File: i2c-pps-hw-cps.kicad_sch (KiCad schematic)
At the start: 1 part, among them U1 BQ25758S

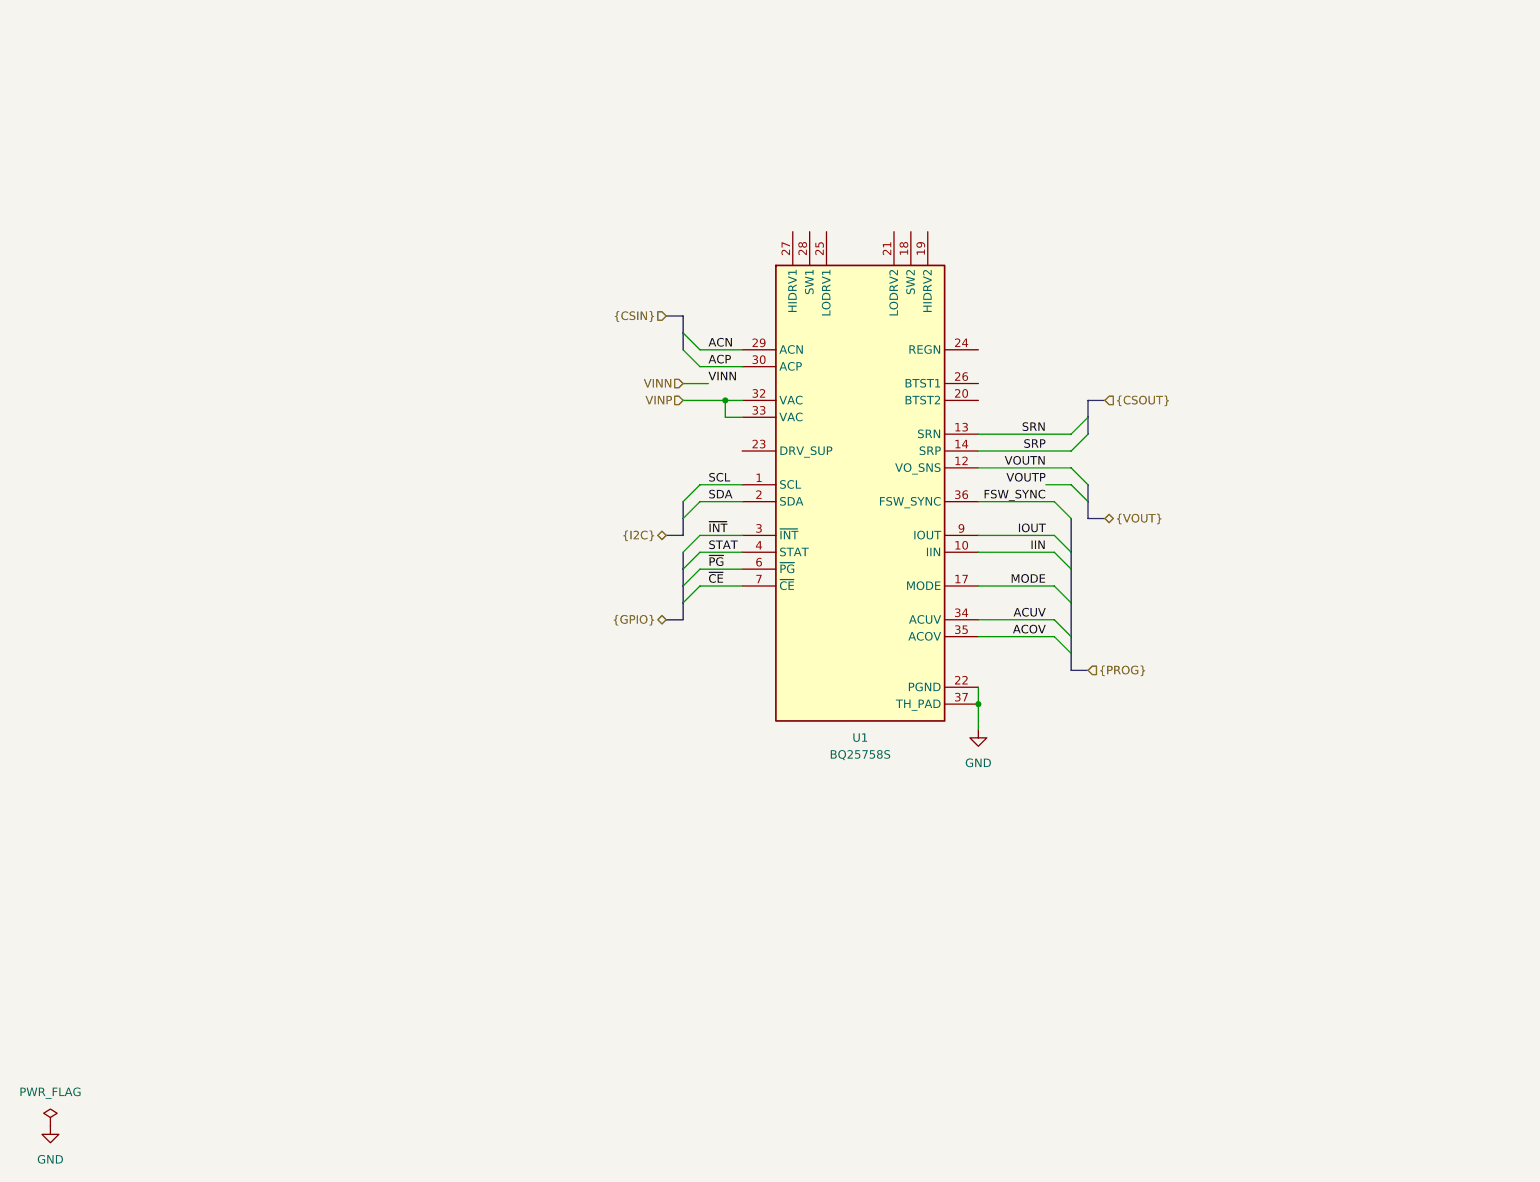
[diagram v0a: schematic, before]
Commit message: Design schematics and set per component requirements
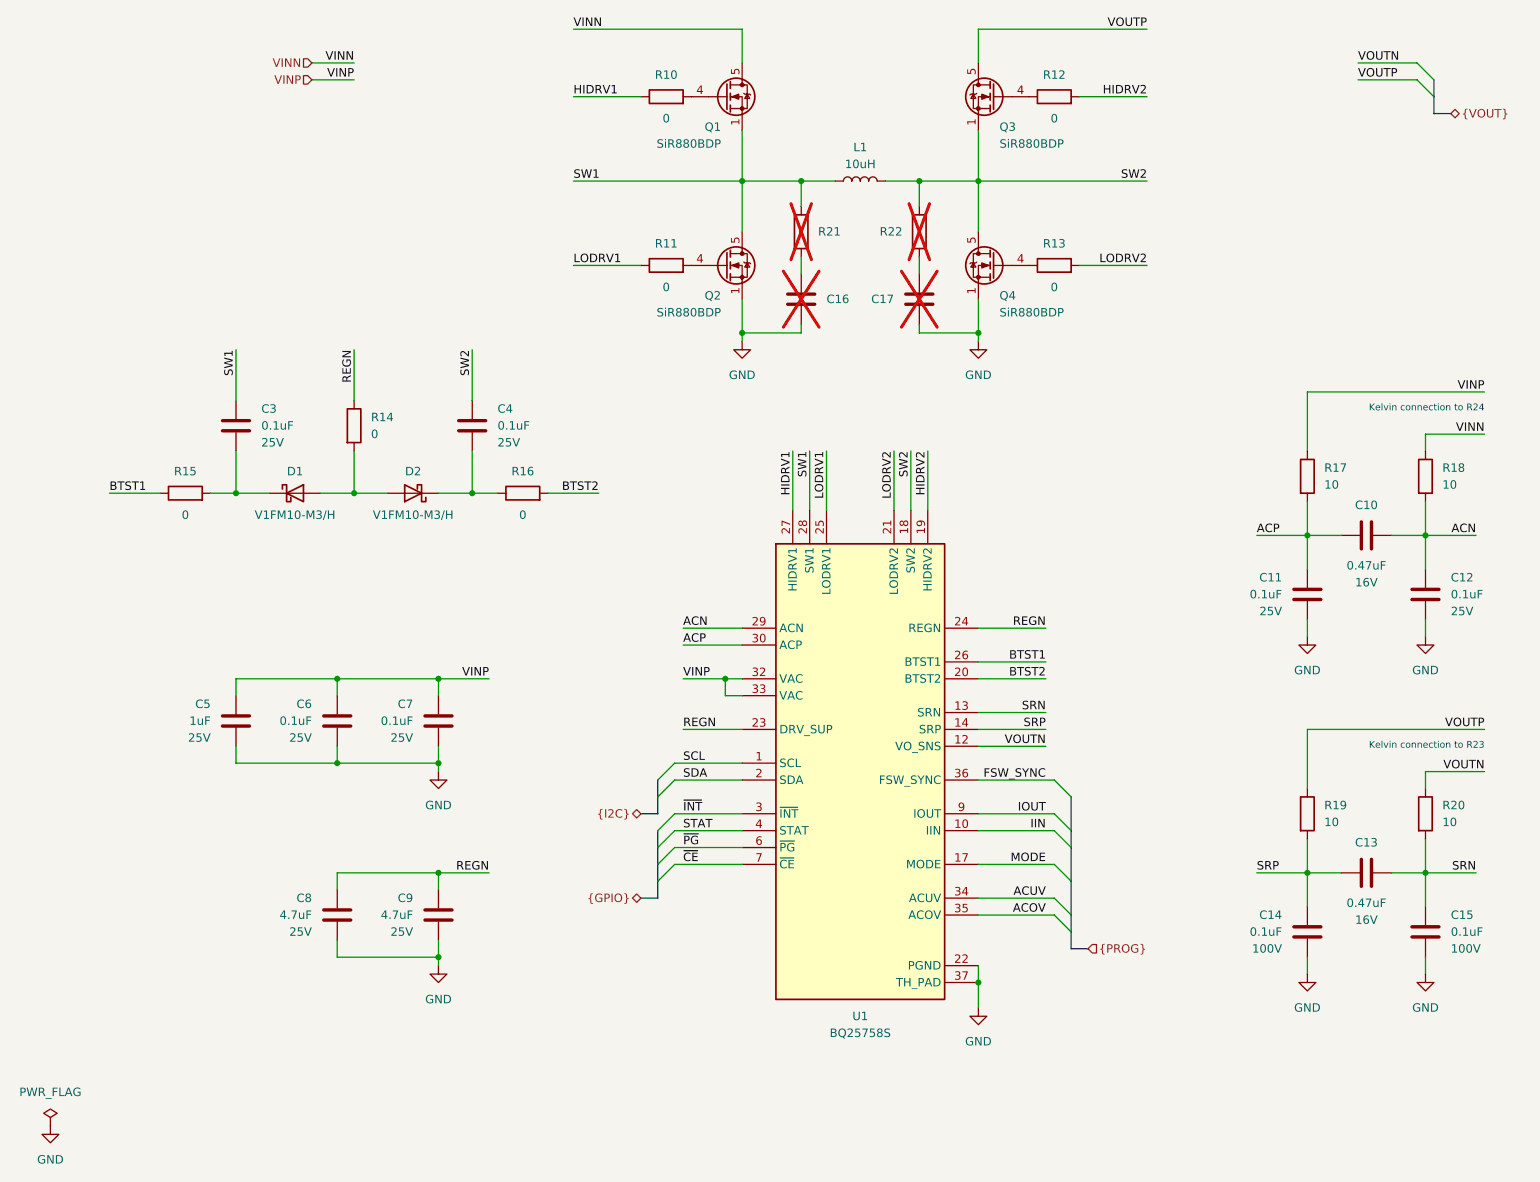
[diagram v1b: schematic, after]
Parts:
- added C10, C13: 0.47uF, Capacitor_SMD:C_0603_1608Metric_Pad1.08x0.95mm_HandSolder, symbol Device:C
- added C11, C12, C14, C15, C3, C4, C6, C7: 0.1uF, Capacitor_SMD:C_0603_1608Metric_Pad1.08x0.95mm_HandSolder, symbol Device:C
- added C16, C17: ~, Capacitor_SMD:C_0805_2012Metric, symbol Device:C
- added C5: 1uF, Capacitor_SMD:C_0805_2012Metric, symbol Device:C
- added C8, C9: 4.7uF, Capacitor_SMD:C_0805_2012Metric, symbol Device:C
- added D1, D2: V1FM10-M3/H, Diode_SMD:D_SMF, symbol Device:D_Schottky
- added L1: 10uH, symbol Device:L
- added Q1, Q2, Q3, Q4: SiR880BDP, Package_SO:PowerPAK_SO-8_Single, symbol i2c-pps-hw:SiR880BDP
- added R10, R11, R12, R13, R15, R16: 0, Resistor_SMD:R_0603_1608Metric_Pad0.98x0.95mm_HandSolder, symbol Device:R
- added R14: 0, Resistor_SMD:R_0805_2012Metric, symbol Device:R
- added R17, R18, R19, R20: 10, Resistor_SMD:R_0603_1608Metric_Pad0.98x0.95mm_HandSolder, symbol Device:R
- added R21, R22: ~, Resistor_SMD:R_1210_3225Metric, symbol Device:R
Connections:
- net ACN: now also C10.1, C12.1, R18.2
- net ACP: now also C10.2, C11.1, R17.2
- net GND: now also C11.2, C12.2, C14.2, C15.2, C16.2, C17.2, C5.2, C6.2, C7.2, C8.2, C9.2, Q2.1 (S), Q2.2 (S), Q2.3 (S), Q4.1 (S), Q4.2 (S), Q4.3 (S)
- net SRN: now also C13.1, C15.1, R20.2
- net SRP: now also C13.2, C14.1, R19.2
- net VINN: now also Q1.5 (D), R18.1
- net VINP: now also C5.1, C6.1, C7.1, R17.1
- net VOUTN: now also R20.1
- net VOUTP: now also Q3.5 (D), R19.1
- net SW2: now reaches U1.18 (SW2)
- net SW2: now also C4.1, L1.2, Q3.1 (S), Q3.2 (S), Q3.3 (S), Q4.5 (D), R22.1
- net HIDRV2: now reaches U1.19 (HIDRV2)
- net HIDRV2: now also R12.2
- net BTST2: now reaches U1.20 (BTST2)
- net BTST2: now also R16.2
- net LODRV2: now reaches U1.21 (LODRV2)
- net LODRV2: now also R13.2
- net REGN: now reaches U1.23 (DRV_SUP)
- net REGN: now also U1.24 (REGN), C8.1, C9.1, R14.1
- net LODRV1: now reaches U1.25 (LODRV1)
- net LODRV1: now also R11.1
- net BTST1: now reaches U1.26 (BTST1)
- net BTST1: now also R15.1
- net HIDRV1: now reaches U1.27 (HIDRV1)
- net HIDRV1: now also R10.1
- net SW1: now reaches U1.28 (SW1)
- net SW1: now also C3.1, L1.1, Q1.1 (S), Q1.2 (S), Q1.3 (S), Q2.5 (D), R21.1
- new net: C4.2, D2.1 (K), R16.1
- new net: D1.2 (A), D2.2 (A), R14.2
- new net: Q4.4 (G), R13.1
- new net: C3.2, D1.1 (K), R15.2
- new net: Q1.4 (G), R10.2
- new net: Q3.4 (G), R12.1
- new net: C16.1, R21.2
- new net: Q2.4 (G), R11.2
- new net: C17.1, R22.2
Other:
- note added: "Kelvin connection to R23"
- note added: "Kelvin connection to R24"
- moved on the sheet: U1

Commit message: Rename VINP to +5V_Run for clarity
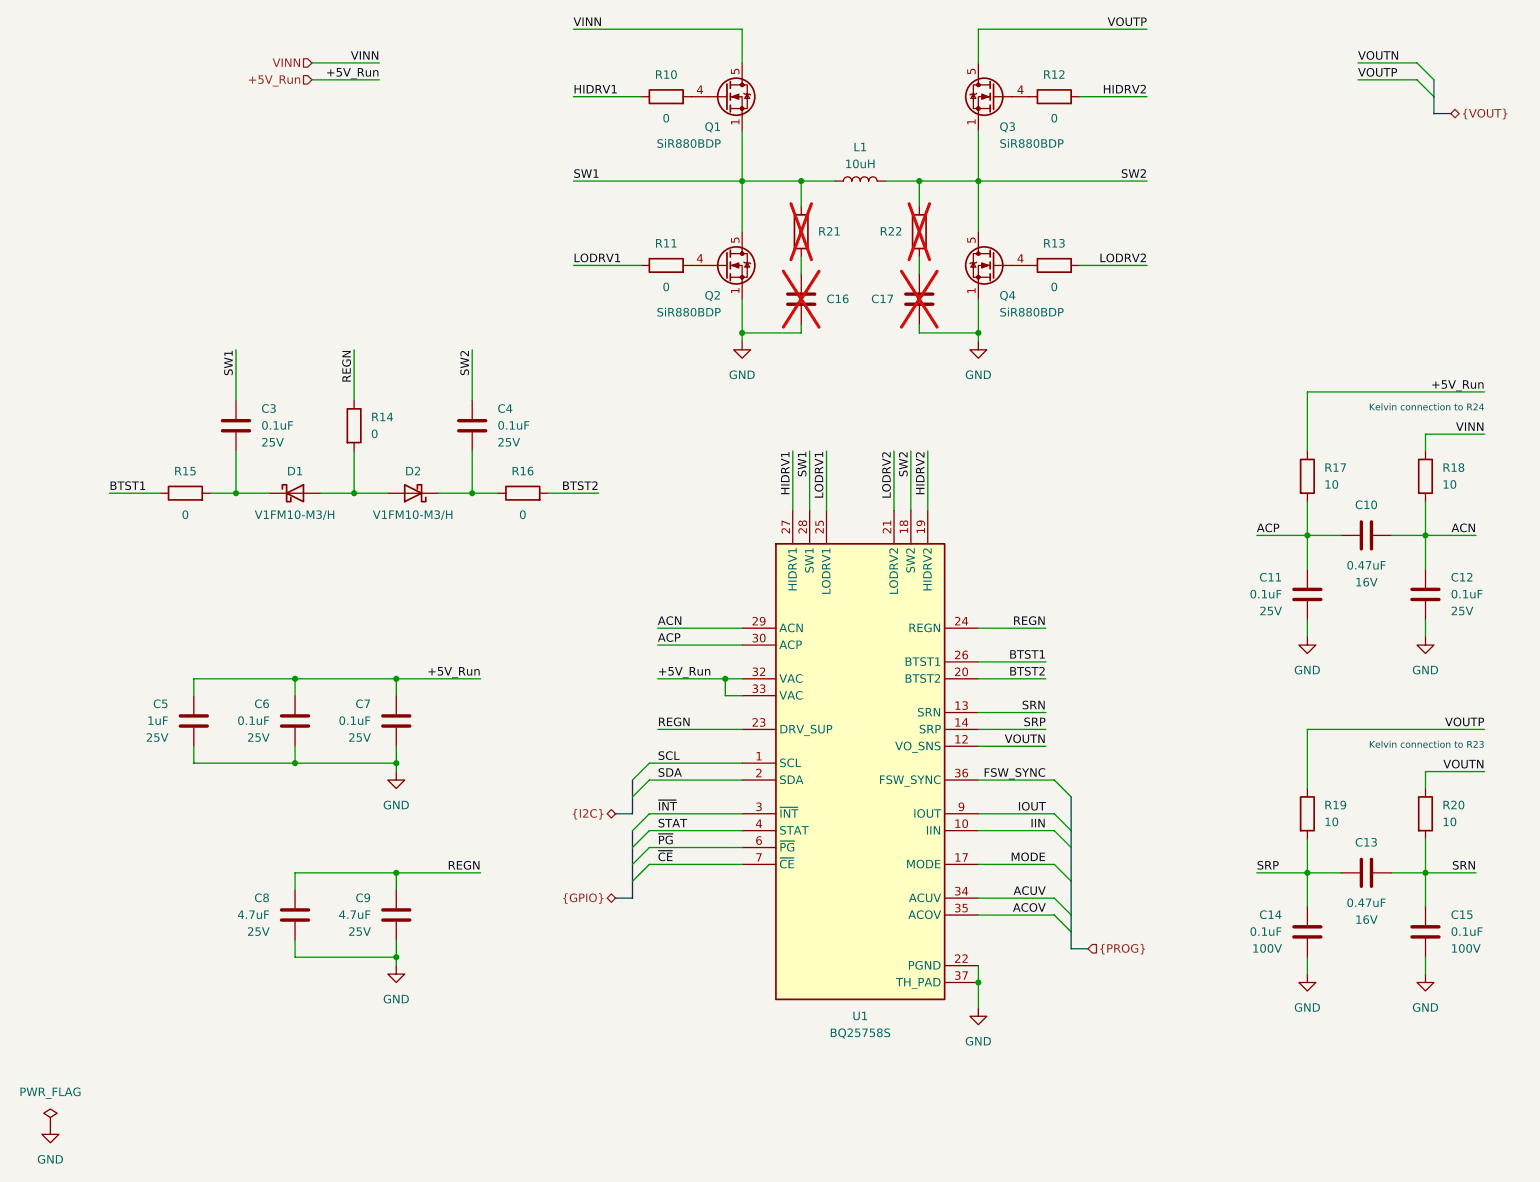
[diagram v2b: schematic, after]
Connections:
- net VINP renamed +5V_Run
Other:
- moved on the sheet: C5, C6, C7, C8, C9

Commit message: Rename VINN to +5V_Filtered for clarity
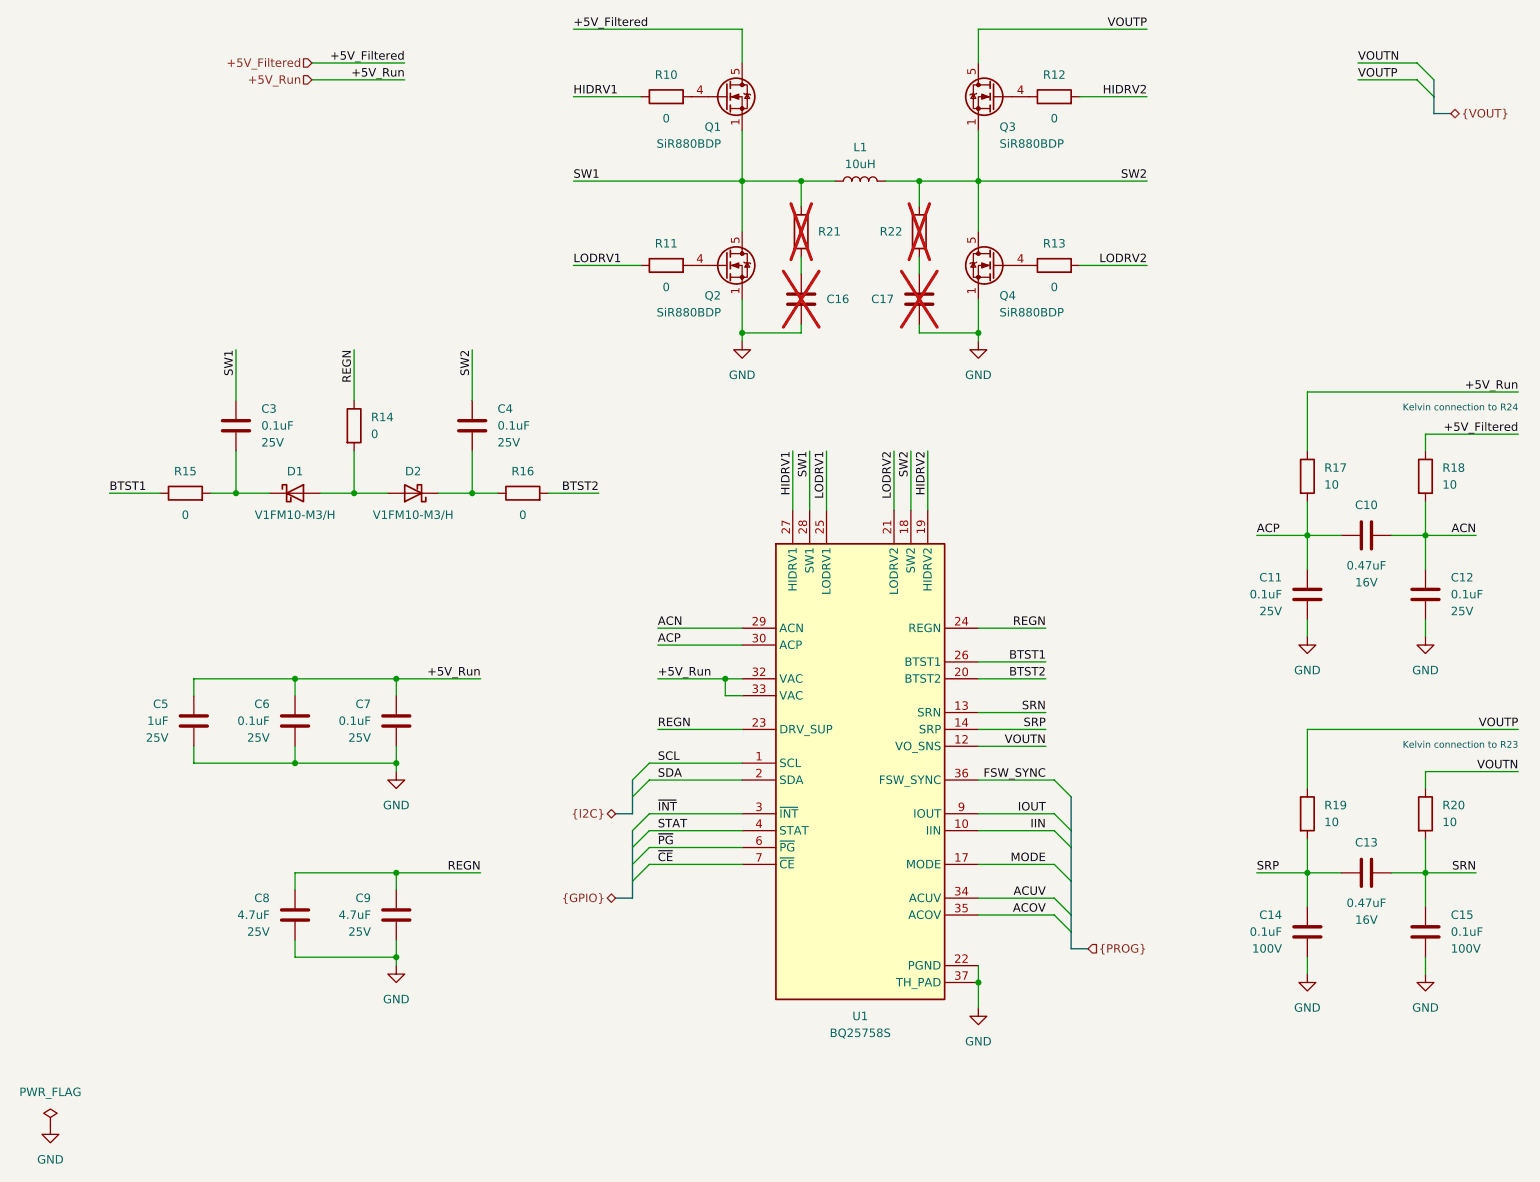
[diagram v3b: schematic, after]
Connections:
- net VINN renamed +5V_Filtered
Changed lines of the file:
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@@
 	(text "Kelvin connection to R24"
 		(exclude_from_sim no)
-		(at 233.68 88.9 0)
+		(at 238.76 88.9 0)
 		(effects
 			(font
@@
 	(text "Kelvin connection to R23"
 		(exclude_from_sim no)
-		(at 233.68 139.7 0)
+		(at 238.76 139.7 0)
 		(effects
 			(font
@@
 	(wire
 		(pts
-			(xy 233.68 86.36) (xy 207.01 86.36)
+			(xy 238.76 86.36) (xy 207.01 86.36)
 		)
 		(stroke
@@
 	(wire
 		(pts
-			(xy 57.15 39.37) (xy 67.31 39.37)
+			(xy 57.15 39.37) (xy 71.12 39.37)
 		)
 		(stroke
@@
 	(wire
 		(pts
-			(xy 233.68 137.16) (xy 207.01 137.16)
+			(xy 238.76 137.16) (xy 207.01 137.16)
 		)
 		(stroke
@@
 	(wire
 		(pts
-			(xy 67.31 36.83) (xy 57.15 36.83)
+			(xy 71.12 36.83) (xy 57.15 36.83)
 		)
 		(stroke
@@
 	(wire
 		(pts
-			(xy 233.68 92.71) (xy 224.79 92.71)
+			(xy 238.76 92.71) (xy 224.79 92.71)
 		)
 		(stroke
@@
 	(wire
 		(pts
-			(xy 233.68 143.51) (xy 224.79 143.51)
+			(xy 238.76 143.51) (xy 224.79 143.51)
 		)
 		(stroke
@@
 		)
 	)
-	(label "VINN"
-		(at 67.31 36.83 180)
+	(label "+5V_Filtered"
+		(at 71.12 36.83 180)
 		(effects
 			(font
@@
 	)
 	(label "+5V_Run"
-		(at 233.68 86.36 180)
+		(at 238.76 86.36 180)
 		(effects
 			(font
@@
 		)
 	)
-	(label "VINN"
-		(at 233.68 92.71 180)
+	(label "+5V_Filtered"
+		(at 238.76 92.71 180)
 		(effects
 			(font
@@
 	)
 	(label "+5V_Run"
-		(at 67.31 39.37 180)
+		(at 71.12 39.37 180)
 		(effects
 			(font
@@
 	)
 	(label "VOUTN"
-		(at 233.68 143.51 180)
+		(at 238.76 143.51 180)
 		(effects
 			(font
@@
 		)
 	)
-	(label "VINN"
+	(label "+5V_Filtered"
 		(at 96.52 31.75 0)
 		(effects
@@
 	)
 	(label "VOUTP"
-		(at 233.68 137.16 180)
+		(at 238.76 137.16 180)
 		(effects
 			(font
@@
 		)
 	)
-	(hierarchical_label "VINN"
+	(hierarchical_label "+5V_Filtered"
 		(shape input)
 		(at 57.15 36.83 180)
